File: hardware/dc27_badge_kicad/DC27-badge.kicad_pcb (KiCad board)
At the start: 4 copper layers, 79.1 x 184.5 mm, 134 parts, among them J101 Conn_ARM_JTAG_SWD_10, J102 ShittyAddOnL, J103 ShittyAddOnR, J104 Conn_02x20_Odd_Even, J601 USB_MICRO_RIGHT, SW108 RESET, SW401 POWER ON, SW801 SKRHAAE010, SW802 SKRHAAE010, U100 BMD-340-A-R-DC27-peripheral-c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, U301 IS31FL3216A, U401 MCP73833, U402 LM1117-3.3, U501 CS4344-CZZ, U502 LM4880, U601 CP2102N-A01-GQFN28, U602 TPD3E001DRLR, Y101 32.768Khz XTAL

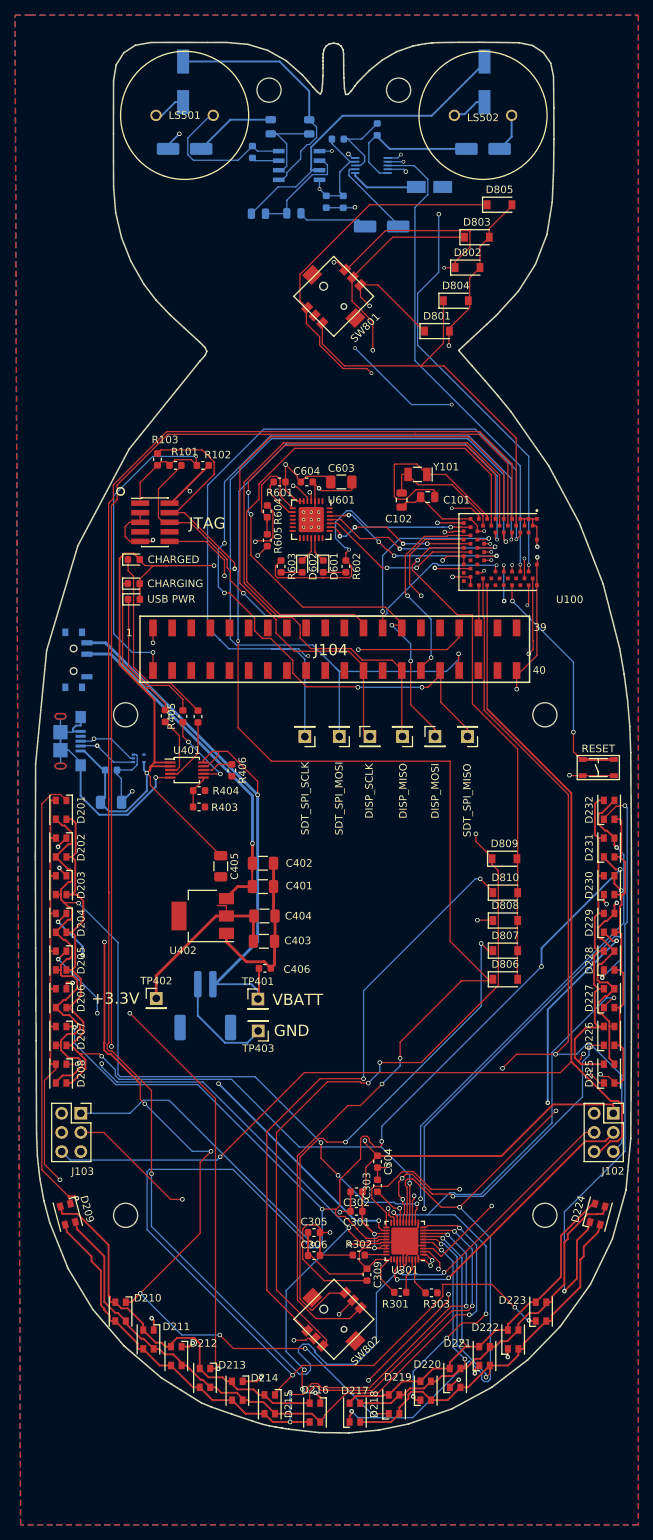
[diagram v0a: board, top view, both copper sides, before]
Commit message: check in latest budget numbers, check in bombface graphics
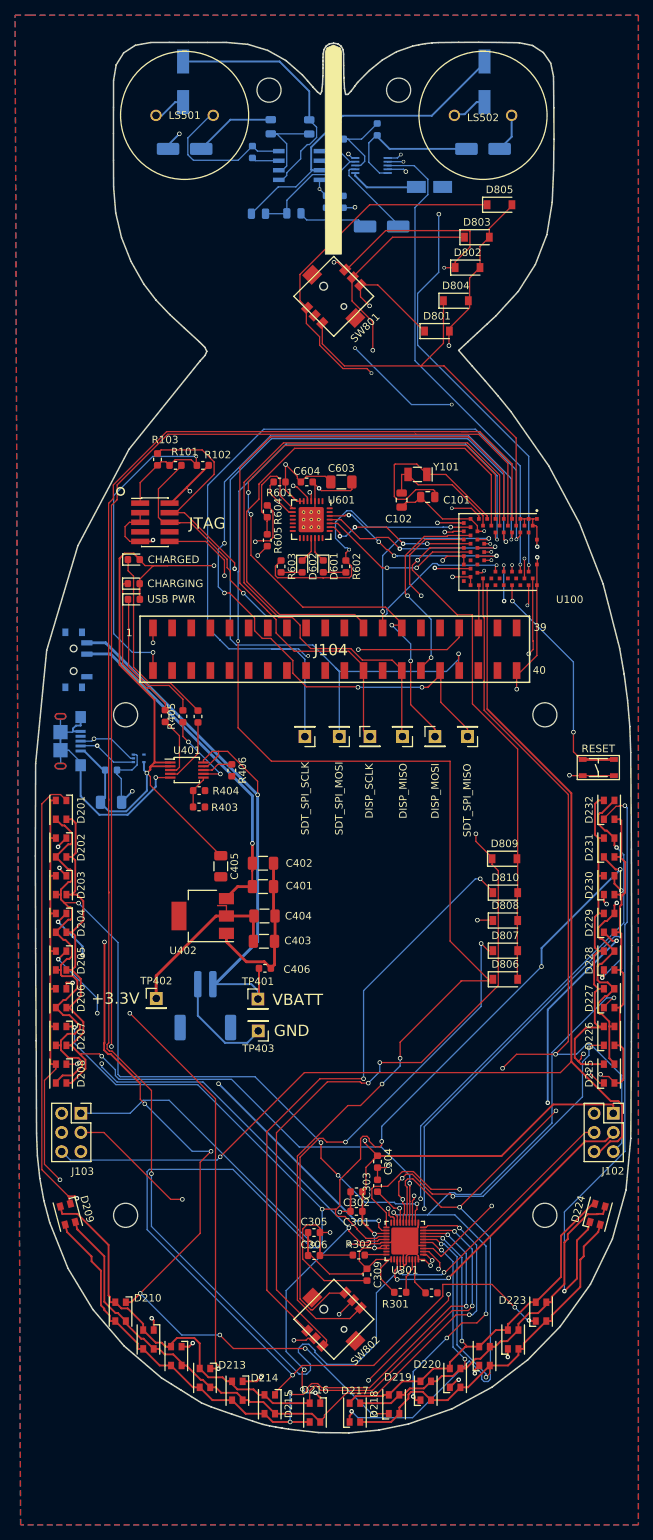
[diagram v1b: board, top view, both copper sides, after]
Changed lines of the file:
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@@
   (general
     (thickness 1.6)
-    (drawings 179)
+    (drawings 180)
     (tracks 2423)
     (zones 0)
@@
     (tags "LED Cree PLCC-4")
     (attr smd)
-    (fp_text reference D222 (at 1.6 -3.7 180) (layer F.SilkS)
+    (fp_text reference D222 (at 1.6 -3.7 180) (layer F.SilkS) hide
       (effects (font (size 1 1) (thickness 0.15)))
     )
@@
     (tags "LED Cree PLCC-4")
     (attr smd)
-    (fp_text reference D221 (at 1.7 -3.6 180) (layer F.SilkS)
+    (fp_text reference D221 (at 1.7 -3.6 180) (layer F.SilkS) hide
       (effects (font (size 1 1) (thickness 0.15)))
     )
@@
     (tags "LED Cree PLCC-4")
     (attr smd)
-    (fp_text reference D212 (at -1.7 -3.6) (layer F.SilkS)
+    (fp_text reference D212 (at -1.7 -3.6) (layer F.SilkS) hide
       (effects (font (size 1 1) (thickness 0.15)))
     )
@@
     (tags "LED Cree PLCC-4")
     (attr smd)
-    (fp_text reference D211 (at -1.7 -3.7) (layer F.SilkS)
+    (fp_text reference D211 (at -1.7 -3.7) (layer F.SilkS) hide
       (effects (font (size 1 1) (thickness 0.15)))
     )
@@
     (tags resistor)
     (attr smd)
-    (fp_text reference R303 (at 0.6775 1.49) (layer F.SilkS)
+    (fp_text reference R303 (at 0.6775 1.49) (layer F.SilkS) hide
       (effects (font (size 1 1) (thickness 0.15)))
     )
@@
     )
   )
+  (gr_poly (pts (xy 104.26 39.8) (xy 105.14 39.41) (xy 106.09 39.82) (xy 106.24 40.41) (xy 106.21 67.17) (xy 104.07 67.17) (xy 104.05 40.41)) (layer F.SilkS) (width 0.1))
   (gr_text +3.3V (at 76.22 165.95) (layer F.SilkS)
     (effects (font (size 1.5 1.5) (thickness 0.3)))

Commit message: PROTOV2 OFF TO MACROFAB
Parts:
- added G***: LOGO, lib_fp:bombface-moved, F.Cu at (105.2, 201.3)
- C406: footprint Capacitor_SMD:C_0603_1608Metric -> Capacitor_SMD:C_1206_3216Metric
- moved D224 22.7 mm to (122.0, 208.1), turned to 60 degrees
- moved D223 17.8 mm to (141.3, 192.0), turned to 82 degrees
- moved D210 11.7 mm to (71.0, 197.4)
- moved D211 11.0 mm to (73.9, 202.5)
- moved D222 9.76 mm to (129.7, 201.5), turned to 75 degrees
- moved D215 9.59 mm to (87.8, 216.2)
- moved D212 9.56 mm to (77.1, 207.1)
- moved D213 9.24 mm to (80.7, 210.8)
- moved D214 9.07 mm to (84.2, 214.0)
- moved D221 7.57 mm to (128.1, 206.4), turned to 55 degrees
- moved D220 7.24 mm to (125.7, 210.6), turned to 65 degrees
- moved D218 6.61 mm to (119.2, 217.1)
- moved D219 6.40 mm to (123.0, 214.9)
- moved J103 5.67 mm to (69.0, 186.2), turned to 180 degrees
- moved R303 4.48 mm to (114.0, 206.7), turned to 180 degrees
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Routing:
- net AVCC: track 332.8 -> 374.9 mm, vias 12 -> 14
- net CS2: track 190.2 -> 212.0 mm, vias 12 -> 13
- net CS7: track 234.1 -> 217.4 mm, vias 8 -> 5
- net CS5: track 232.1 -> 216.1 mm, vias 8 -> 10
- net CS4: track 213.5 -> 229.0 mm, vias 9 -> 7
- net SW5: track 73.7 -> 83.6 mm, vias 2 -> 5
- net CS6: track 188.0 -> 178.7 mm
- net CS3: track 195.5 -> 203.5 mm
- net SW4: track 69.4 -> 76.6 mm, vias 2 -> 4
- net SW9: track 92.2 -> 97.9 mm, vias 2 -> 4
- net SW11: track 109.1 -> 104.3 mm
- net SW6: track 66.1 -> 70.6 mm, vias 2 -> 3
- net SW8: track 96.2 -> 92.5 mm
- net I2C_SDA: track 242.7 -> 245.9 mm
- net Net-(C401-Pad1): track 46.0 -> 48.9 mm
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
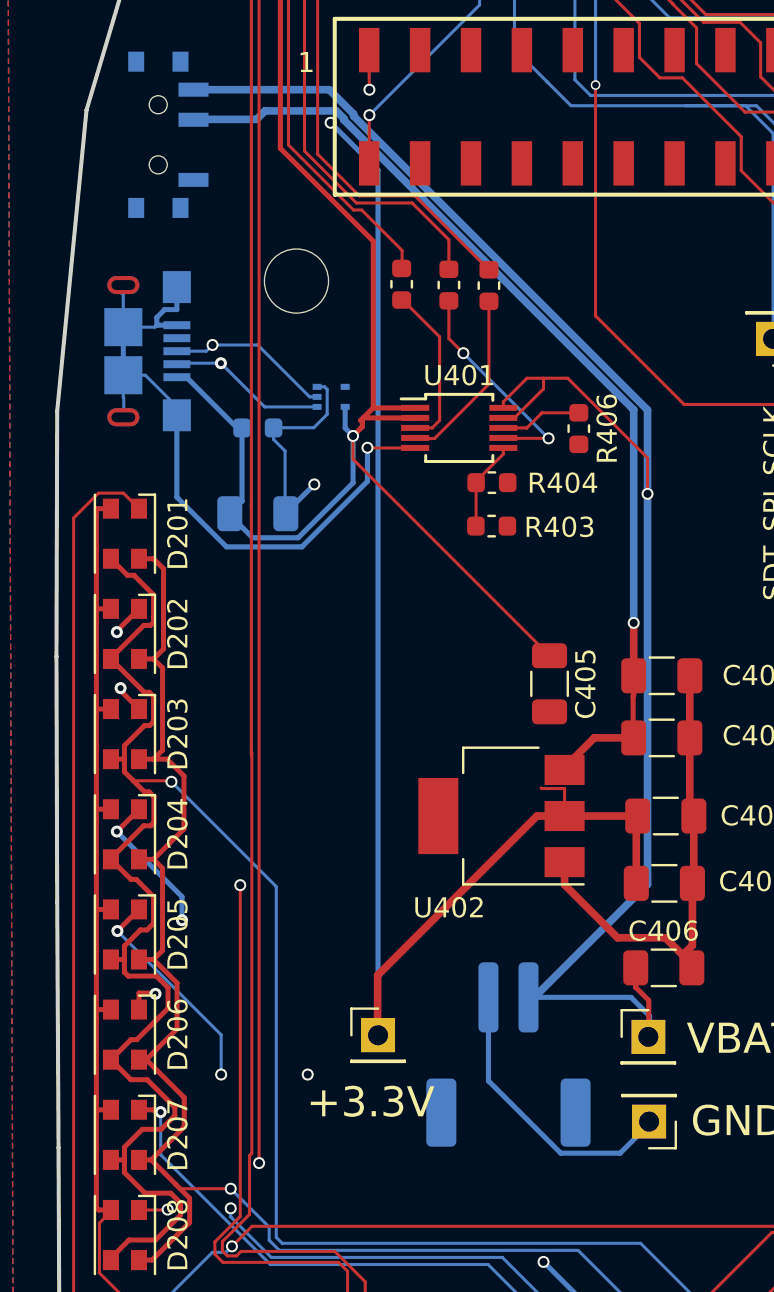
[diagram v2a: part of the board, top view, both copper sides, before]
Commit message: move c405 closer to the battery power circuit make a bunch of ground traces 0.254 instead of 0.152 sized to improve grounding
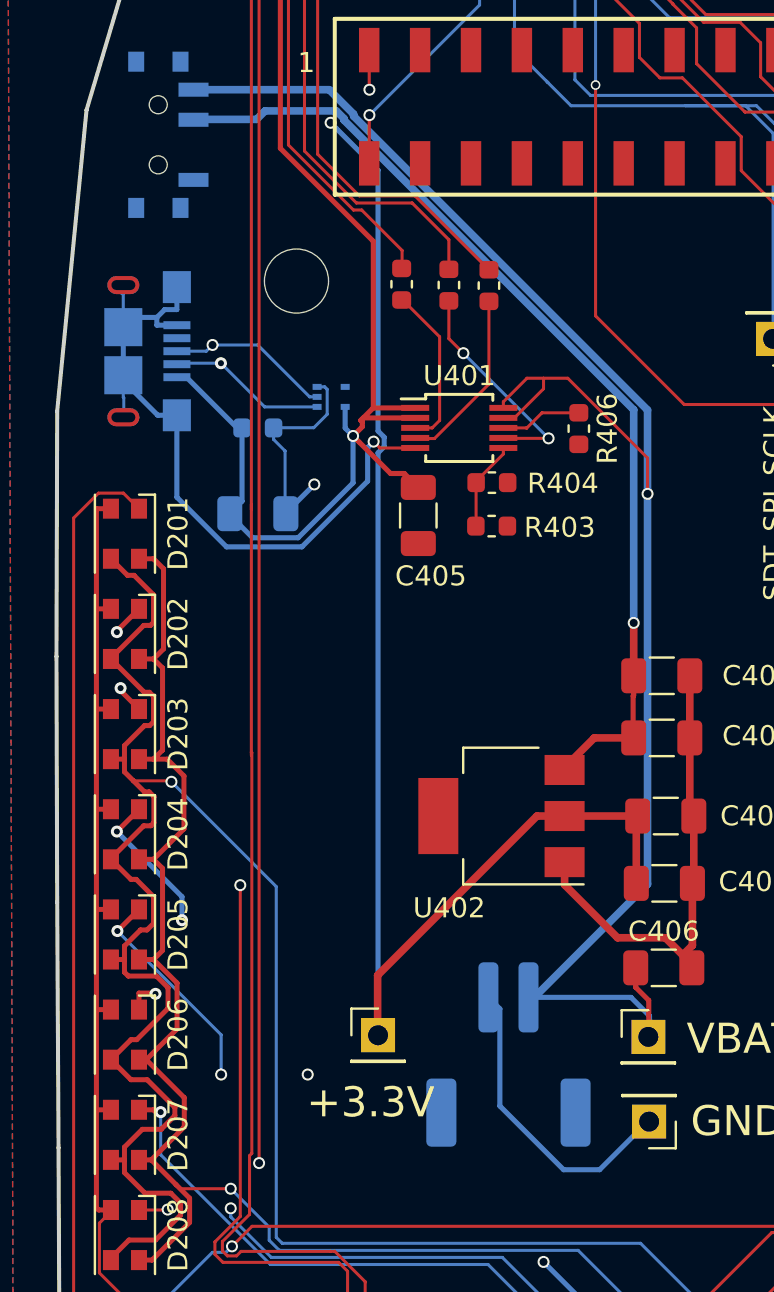
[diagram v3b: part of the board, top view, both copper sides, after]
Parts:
- moved C405 10.7 mm to (83.7, 140.0)
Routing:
- net VBUS: track 105.5 -> 94.8 mm
- net AVCC: track 374.9 -> 372.6 mm
- net GND: track 269.2 -> 271.2 mm
